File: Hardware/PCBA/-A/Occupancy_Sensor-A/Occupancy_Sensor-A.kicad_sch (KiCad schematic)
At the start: 67 parts, among them J1 USB_C_Receptacle, J2 Conn_02x05_Odd_Even, Q1 2N7002, Q2 2N7002, Q3 2N7002, Q4 2N7002, Q5 2N7002, SW1 SW_SPDT, SW2 SW_Push, U1 TPS7A0333PDBVR, U2 VL53L8CX, U3 ECMF02-2AMX6, U4 TPS7A03185PDQNR, U5 TCS3430, U6 STM32WB55CGUx, Y2 NX2016SA_32M, Y3 NX2012_32K768

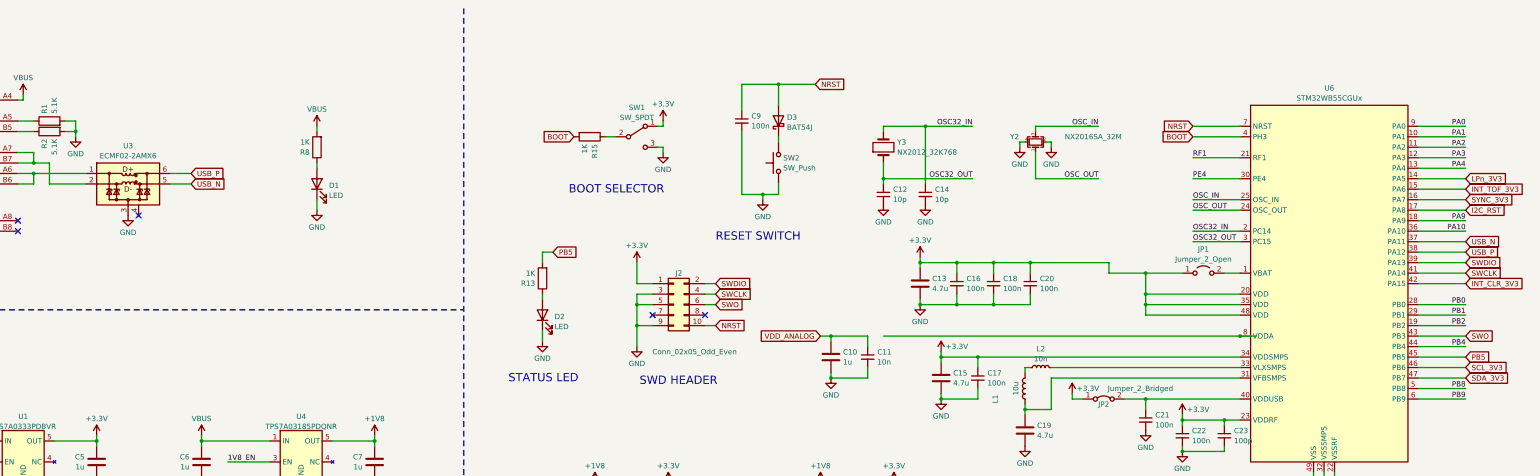
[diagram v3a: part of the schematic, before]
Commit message: Layout cleanup, silk fixes
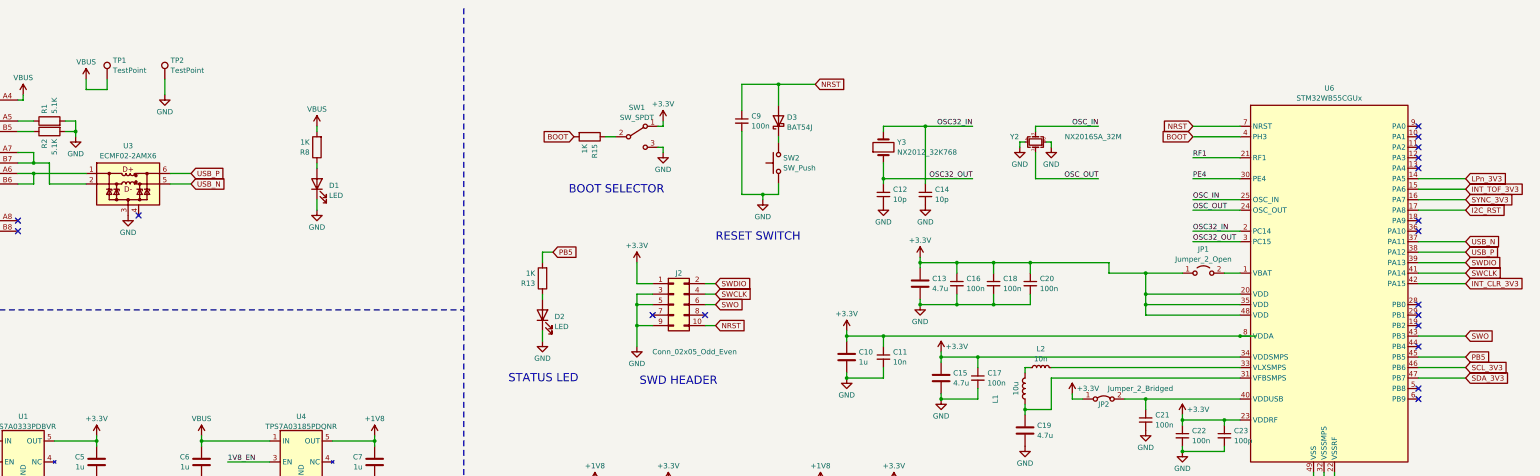
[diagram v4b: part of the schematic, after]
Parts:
- added TP1, TP2: TestPoint, TestPoint:TestPoint_Pad_D2.0mm, symbol Connector:TestPoint
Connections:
- net VDD_ANALOG is gone; now on net +3.3V: C10.1, C11.1
- net +3.3V: now also U6.8 (VDDA)
- net GND: now also TP2.1
- net VBUS: now also TP1.1
- net PA0: no longer names the net of U6.9 (PA0)
- net PA1: no longer names the net of U6.10 (PA1)
- net PA10: no longer names the net of U6.36 (PA10)
- net PA2: no longer names the net of U6.11 (PA2)
- net PA3: no longer names the net of U6.12 (PA3)
- net PA4: no longer names the net of U6.13 (PA4)
- net PA9: no longer names the net of U6.18 (PA9)
- net PB0: no longer names the net of U6.28 (PB0)
- net PB1: no longer names the net of U6.29 (PB1)
- net PB2: no longer names the net of U6.19 (PB2)
- net PB4: no longer names the net of U6.44 (PB4)
- net PB8: no longer names the net of U6.5 (PB8)
- net PB9: no longer names the net of U6.6 (PB9)
- no-connect marks 7 -> 20
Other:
- moved on the sheet: C10, C11

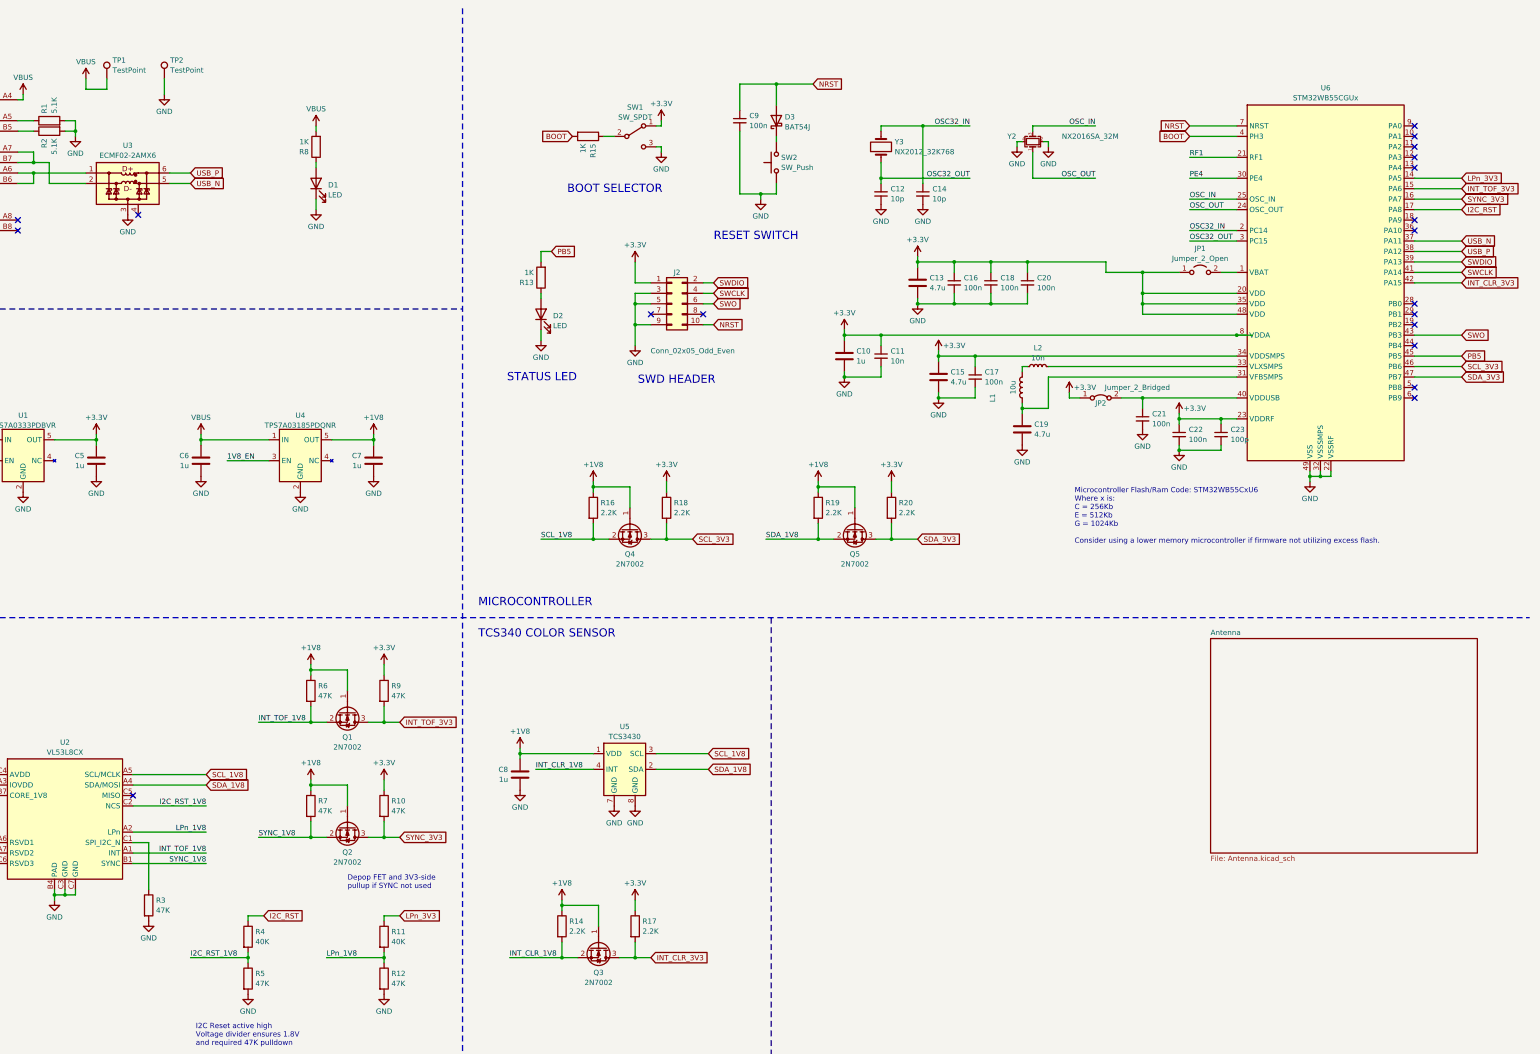
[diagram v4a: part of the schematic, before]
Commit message: Layout fixes, boot selector, testpoints
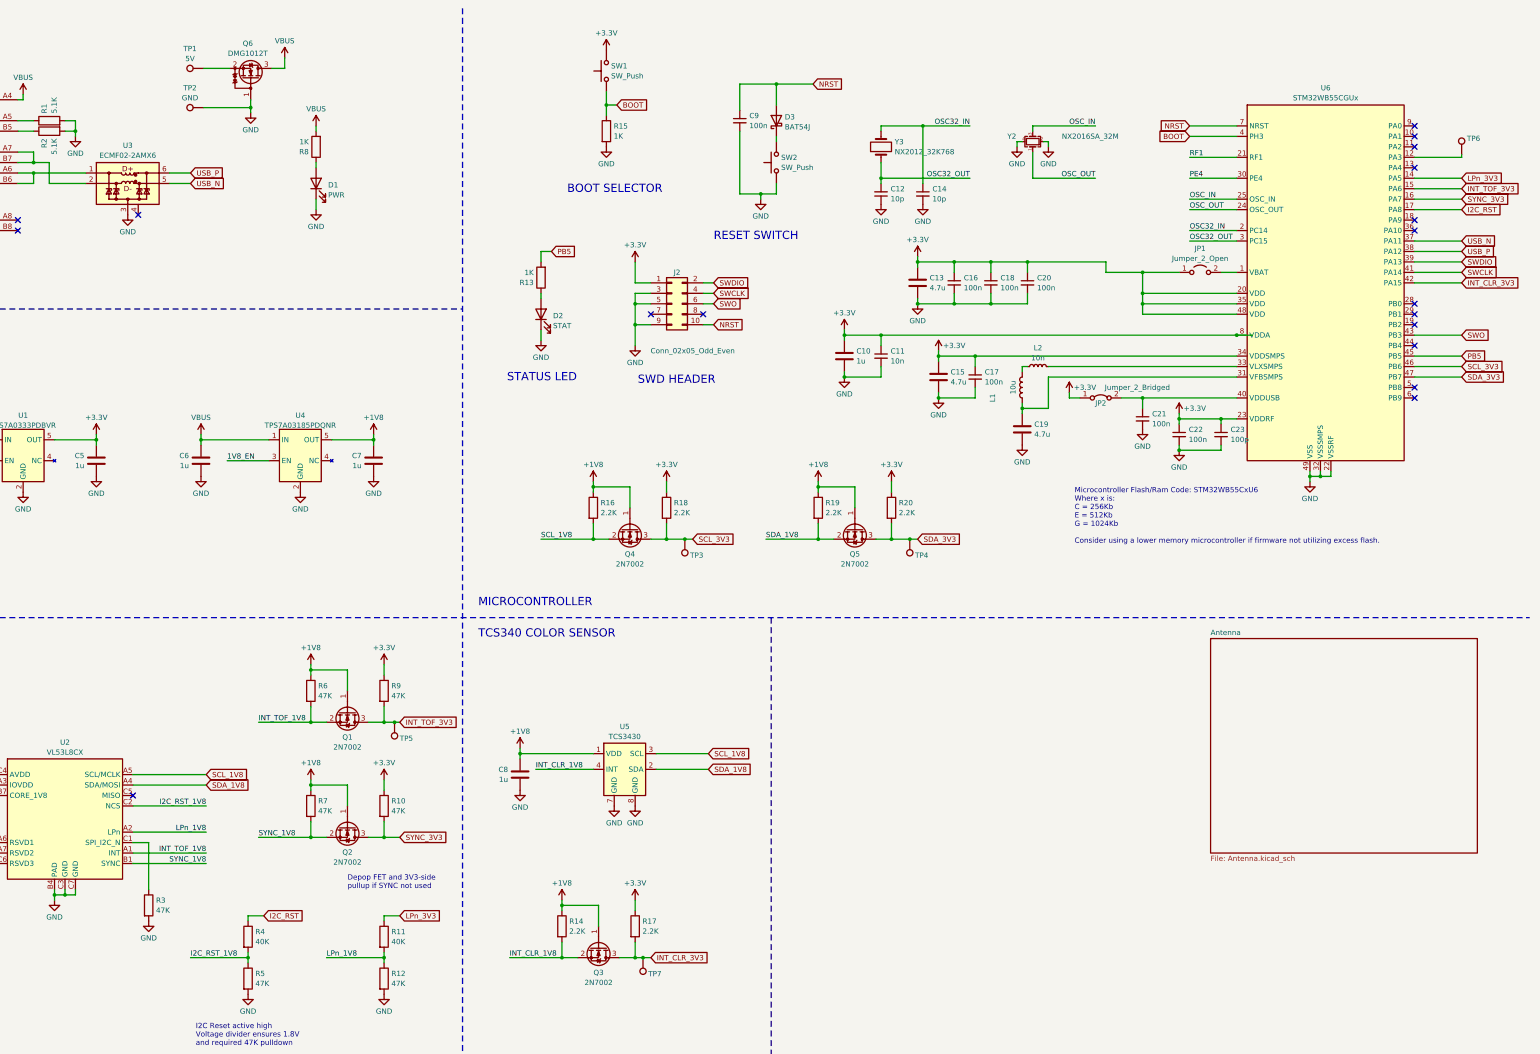
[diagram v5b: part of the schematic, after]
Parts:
- removed SW1: SW_SPDT, Button_Switch_SMD:SW_SPDT_CK-JS102011SAQN, symbol Switch:SW_SPDT
- added Q6: DMG1012T, Package_TO_SOT_SMD:SOT-523, symbol Transistor_FET:DMG1012T
- added SW1: SW_Push, Button_Switch_SMD:SW_Push_SPST_NO_Alps_SKRK, symbol Switch:SW_Push
- added TP3: SCL, TestPoint:TestPoint_Pad_D1.0mm, symbol Connector:TestPoint
- added TP4: SDA, TestPoint:TestPoint_Pad_D1.0mm, symbol Connector:TestPoint
- added TP5: INTT, TestPoint:TestPoint_Pad_D1.0mm, symbol Connector:TestPoint
- added TP6: PA3, TestPoint:TestPoint_Pad_D1.0mm, symbol Connector:TestPoint
- added TP7: INTC, TestPoint:TestPoint_Pad_D1.0mm, symbol Connector:TestPoint
- D1: value LED -> PWR
- D2: value LED -> STAT
- TP1: value TestPoint -> 5V
- TP2: value TestPoint -> GND
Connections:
- net +3.3V: now also SW1.2
- net BOOT: now also R15.1, SW1.1; no longer R15.2
- net GND: now also R15.2, Q6.1 (G)
- net INT_CLR_3V3: now also TP7.1
- net INT_TOF_3V3: now also TP5.1
- net SCL_3V3: now also TP3.1
- net SDA_3V3: now also TP4.1
- net VBUS: now also Q6.3 (D); no longer TP1.1
- net at U6.12 (PA3): now also TP6.1
- new net: Q6.2 (S), TP1.1
- no-connect marks 20 -> 19
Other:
- moved on the sheet: R15, TP1, TP2

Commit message: RF layout
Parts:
- added C24: 0.8pf, Capacitor_SMD:C_0402_1005Metric, symbol Device:C_Small
- added C25: 0.3pf, Capacitor_SMD:C_0402_1005Metric, symbol Device:C_Small
- added C26: 10nf, Capacitor_SMD:C_0402_1005Metric, symbol Device:C_Small
- added C27: 1.2pf, Capacitor_SMD:C_0402_1005Metric, symbol Device:C_Small
- added C28: ~, Capacitor_SMD:C_0402_1005Metric, symbol Device:C_Small
- added J3: Conn_Coaxial, Connector_Coaxial:U.FL_Molex_MCRF_73412-0110_Vertical, symbol Connector:Conn_Coaxial
- added L3: 2.7nH, Inductor_SMD:L_0402_1005Metric, symbol Device:L
- added L4: 3.6nH, Inductor_SMD:L_0402_1005Metric, symbol Device:L
- added U7: ~, Occupancy_Sensor_Custom_Footprints:LFB182G45CGFD436, symbol Occupancy_Sensor_Custom_Symbols:LFB182G45CGFD436
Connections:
- net GND: now also C24.2, C25.2, C27.2, C28.2, J3.2 (Ext), U7.2 (GND)
- net RF1 renamed RF
- net RF: now also C24.1, L3.1
- new net: C25.1, L3.2, U7.1
- new net: C26.1, U7.3
- new net: C26.2, C28.1, L4.1
- new net: C27.1, J3.1 (In), L4.2
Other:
- removed sheet Antenna
- note added: "Antenna Band Filter"
- moved on the sheet: C8, Q3, R14, R17, TP7, U5

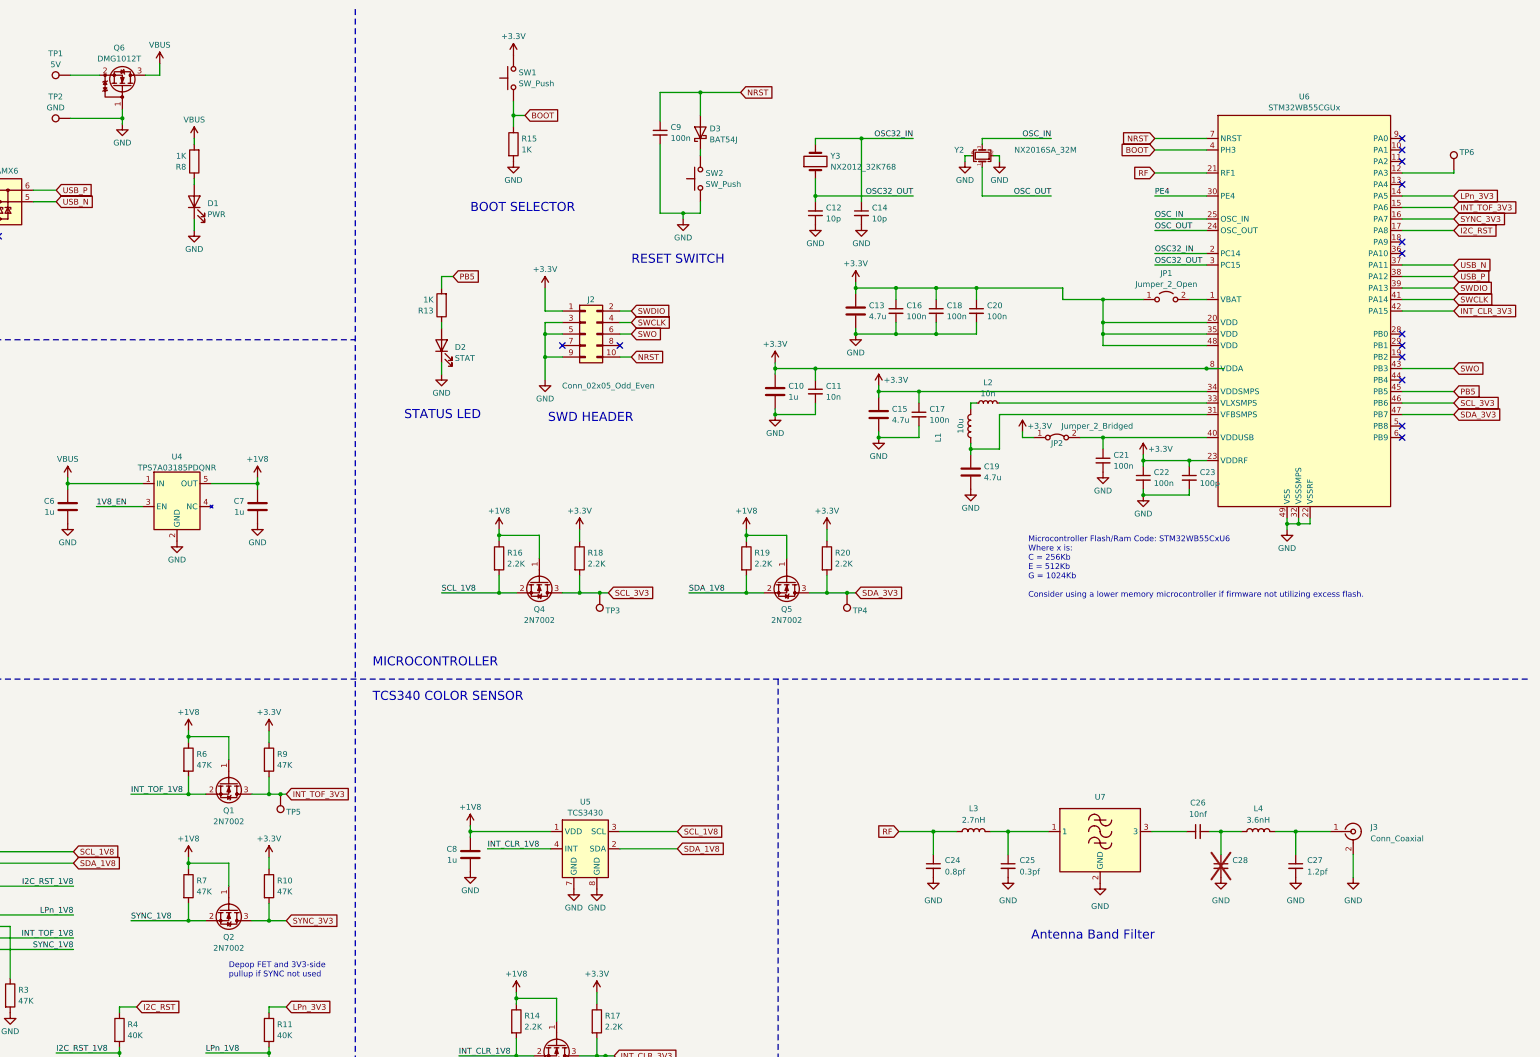
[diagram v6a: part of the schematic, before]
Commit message: Final TOF sensor layout
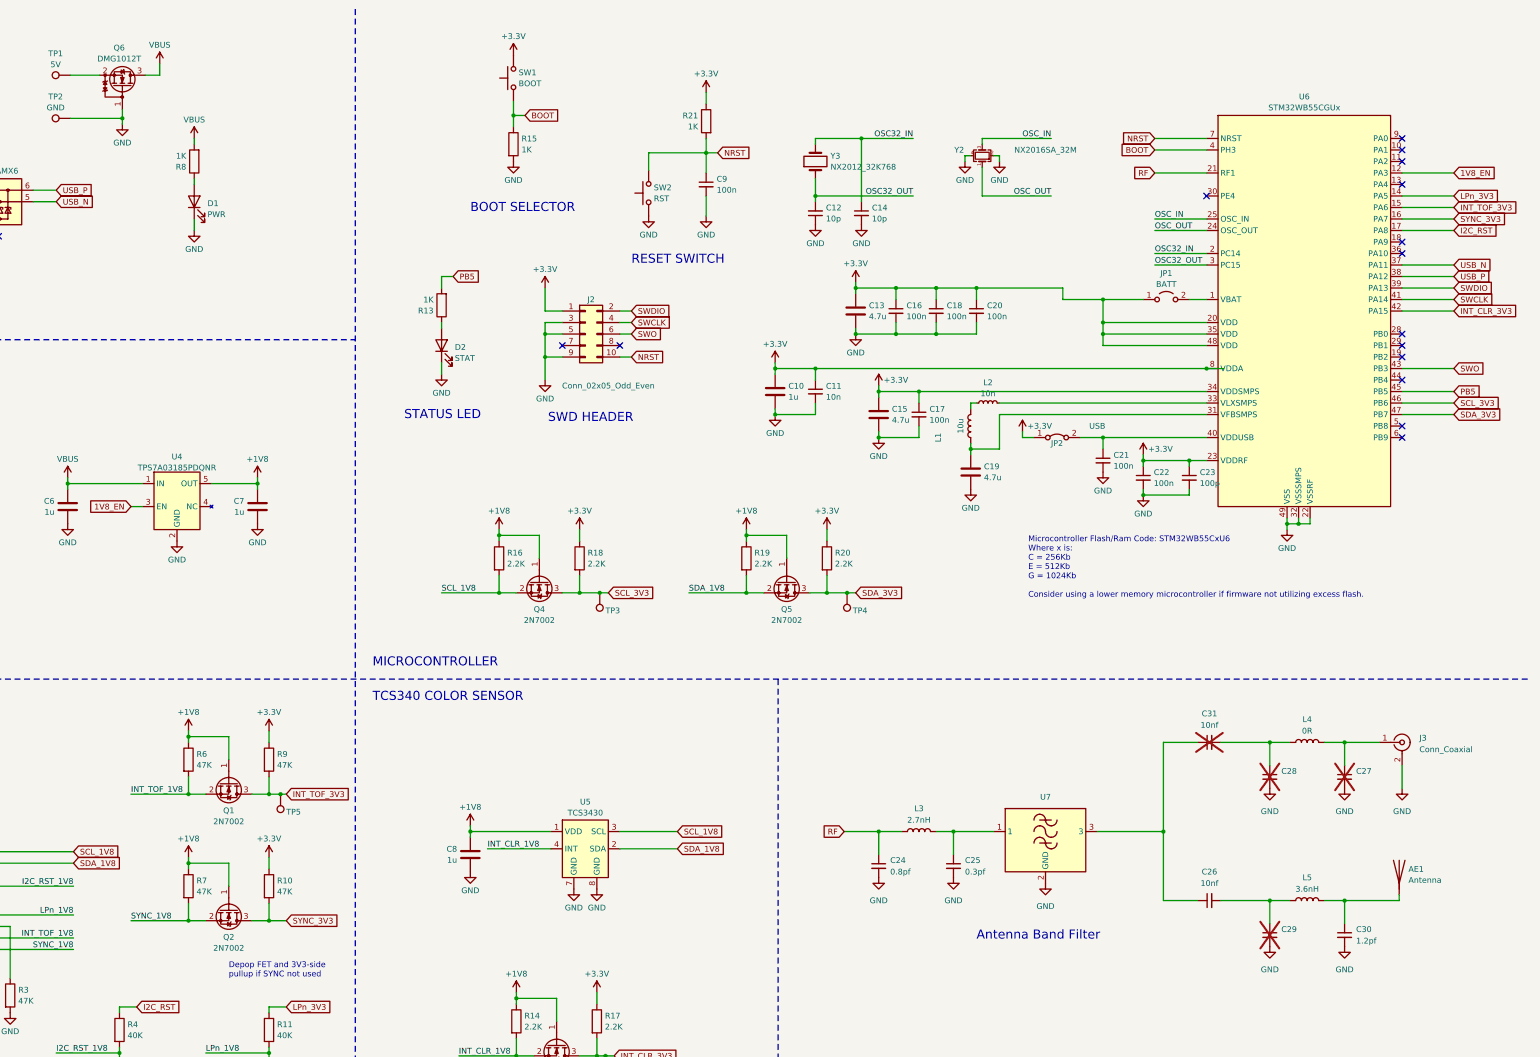
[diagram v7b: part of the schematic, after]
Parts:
- removed D3: BAT54J, Diode_SMD:D_SOD-323F, symbol Diode:BAT54J
- removed TP6: PA3, TestPoint:TestPoint_Pad_D1.0mm, symbol Connector:TestPoint
- added AE1: Antenna, Occupancy_Sensor_Custom_Footprints:AN3359_Meander_Antenna, symbol Device:Antenna
- added C29: ~, Capacitor_SMD:C_0402_1005Metric, symbol Device:C_Small
- added C30: 1.2pf, Capacitor_SMD:C_0402_1005Metric, symbol Device:C_Small
- added C31: 10nf, Capacitor_SMD:C_0402_1005Metric, symbol Device:C_Small
- added L5: 3.6nH, Inductor_SMD:L_0603_1608Metric, symbol Device:L
- added R21: 1K, Resistor_SMD:R_0402_1005Metric, symbol Device:R
- C27: value 1.2pf -> ~; now not fitted
- J1: footprint Occupancy_Sensor_Custom_Footprints:TYPEC-304S-ACP16 -> Occupancy_Sensor_Custom_Footprints:USB4110-GF-A
- JP1: value Jumper_2_Open -> BATT
- JP2: value Jumper_2_Bridged -> USB
- L4: value 3.6nH -> 0R; footprint Inductor_SMD:L_0402_1005Metric -> Resistor_SMD:R_0603_1608Metric
- SW1: value SW_Push -> BOOT
- SW2: value SW_Push -> RST
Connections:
- net +3.3V: now also R21.1
- net 1V8_EN: now also U6.12 (PA3)
- net GND: now also C29.2, C30.2
- net NRST: now also SW2.2, R21.2
- net at C26.1, U7.3: now also C31.1
- net at C28.1, L4.1: now also C31.2; no longer C26.2
- net PE4: no longer names the net of U6.30 (PE4)
- new net: AE1.1 (A), C30.1, L5.2
- new net: C26.2, C29.1, L5.1
- no-connect marks 19 -> 20
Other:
- moved on the sheet: C24, C25, C26, C28, C9, J3, L3, L4, SW2, U7
